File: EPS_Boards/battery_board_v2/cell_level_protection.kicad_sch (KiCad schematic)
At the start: 32 parts, among them J8 Shunt Resistor, Q10 CSD16401Q5, Q3 CSD16401Q5, Q4 CSD16401Q5, Q5 CSD16401Q5, Q6 CSD16401Q5, Q7 CSD16401Q5, Q8 CSD16401Q5, Q9 CSD16401Q5, U10 BQ297xx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

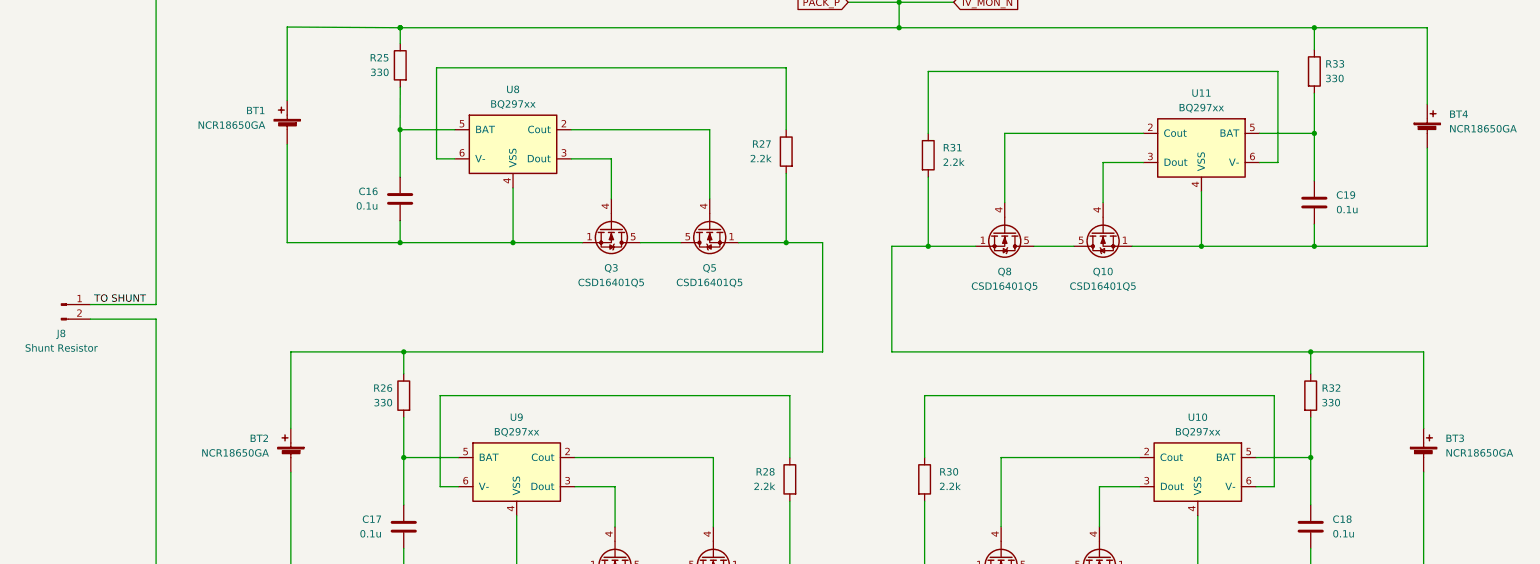
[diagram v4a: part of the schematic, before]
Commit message: eps: battery board: updated board layout
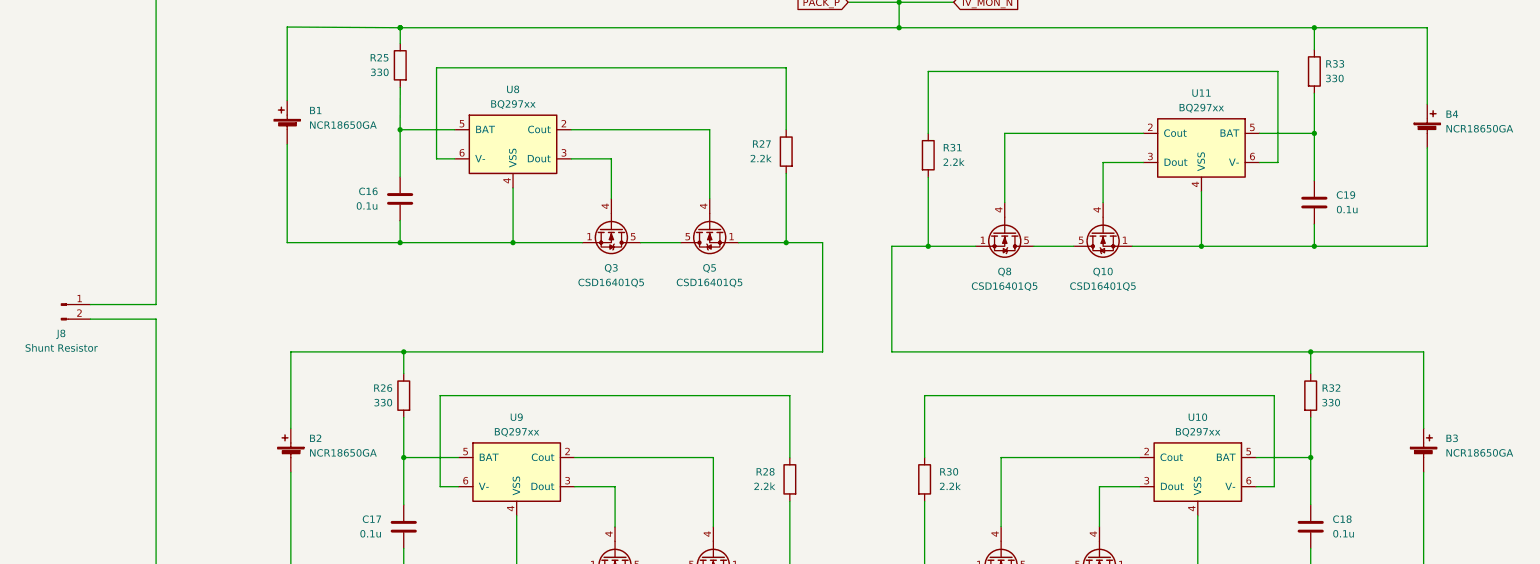
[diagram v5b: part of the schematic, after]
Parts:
- C16, C17, C18, C19: footprint (none) -> Capacitor_SMD:C_0402_1005Metric
- F1, F2: footprint (none) -> Capacitor_Tantalum_SMD:CP_EIA-7132-20_AVX-U_Pad2.72x3.50mm_HandSolder
- R25, R26, R27, R28, R29, R30, R31, R32, R33: footprint (none) -> Resistor_SMD:R_0402_1005Metric
- renumbered BT1 to B1, BT2 to B2, BT3 to B3, BT4 to B4
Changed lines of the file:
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@@
-    (effects (font (size 1.27 1.27)) (justify left bottom))
-  )
-  (label "TO SHUNT" (at 86.995 154.94 0)
     (effects (font (size 1.27 1.27)) (justify left bottom))
   )
@@
       (effects (font (size 1.27 1.27)) (justify left))
     )
-    (property "Footprint" "" (id 2) (at 210.058 185.42 90)
+    (property "Footprint" "Resistor_SMD:R_0402_1005Metric" (id 2) (at 210.058 185.42 90)
       (effects (font (size 1.27 1.27)) hide)
     )
@@
       (effects (font (size 1.27 1.27)) (justify right))
     )
-    (property "Footprint" "" (id 2) (at 298.7548 133.35 0)
+    (property "Footprint" "Capacitor_SMD:C_0402_1005Metric" (id 2) (at 298.7548 133.35 0)
       (effects (font (size 1.27 1.27)) hide)
     )
@@
       (effects (font (size 1.27 1.27)) (justify right))
     )
-    (property "Footprint" "" (id 2) (at 141.3002 132.715 0)
+    (property "Footprint" "Capacitor_SMD:C_0402_1005Metric" (id 2) (at 141.3002 132.715 0)
       (effects (font (size 1.27 1.27)) hide)
     )
@@
       (effects (font (size 1.27 1.27)) (justify left))
     )
-    (property "Footprint" "" (id 2) (at 297.307 170.815 90)
+    (property "Footprint" "Resistor_SMD:R_0402_1005Metric" (id 2) (at 297.307 170.815 90)
       (effects (font (size 1.27 1.27)) hide)
     )
@@
   (symbol (lib_id "Device:Battery_Cell") (at 121.285 181.61 0) (mirror y) (unit 1)
     (in_bom yes) (on_board yes) (fields_autoplaced)
-    (property "Reference" "BT2" (id 0) (at 117.475 178.3079 0)
-      (effects (font (size 1.27 1.27)) (justify left))
-    )
-    (property "Value" "NCR18650GA" (id 1) (at 117.475 180.8479 0)
-      (effects (font (size 1.27 1.27)) (justify left))
+    (property "Reference" "B2" (id 0) (at 124.46 178.3079 0)
+      (effects (font (size 1.27 1.27)) (justify right))
+    )
+    (property "Value" "NCR18650GA" (id 1) (at 124.46 180.8479 0)
+      (effects (font (size 1.27 1.27)) (justify right))
     )
     (property "Footprint" "qset-footprints:Keystone_54_18650" (id 2) (at 121.285 180.086 90)
@@
       (effects (font (size 1.27 1.27)) (justify left))
     )
-    (property "Footprint" "" (id 2) (at 297.942 114.3 90)
+    (property "Footprint" "Resistor_SMD:R_0402_1005Metric" (id 2) (at 297.942 114.3 90)
       (effects (font (size 1.27 1.27)) hide)
     )
@@
   (symbol (lib_id "Device:Battery_Cell") (at 318.77 181.61 0) (unit 1)
     (in_bom yes) (on_board yes) (fields_autoplaced)
-    (property "Reference" "BT3" (id 0) (at 322.58 178.3079 0)
+    (property "Reference" "B3" (id 0) (at 322.58 178.3079 0)
       (effects (font (size 1.27 1.27)) (justify left))
     )
@@
       (effects (font (size 1.27 1.27)) (justify left))
     )
-    (property "Footprint" "" (id 2) (at 229.997 185.42 90)
+    (property "Footprint" "Resistor_SMD:R_0402_1005Metric" (id 2) (at 229.997 185.42 90)
       (effects (font (size 1.27 1.27)) hide)
     )
@@
       (effects (font (size 1.27 1.27)) (justify left))
     )
-    (property "Footprint" "" (id 2) (at 230.632 128.905 90)
+    (property "Footprint" "Resistor_SMD:R_0402_1005Metric" (id 2) (at 230.632 128.905 90)
       (effects (font (size 1.27 1.27)) hide)
     )
@@
       (effects (font (size 1.27 1.27)) (justify right))
     )
-    (property "Footprint" "" (id 2) (at 141.9352 189.865 0)
+    (property "Footprint" "Capacitor_SMD:C_0402_1005Metric" (id 2) (at 141.9352 189.865 0)
       (effects (font (size 1.27 1.27)) hide)
     )
@@
       (effects (font (size 1.27 1.27)) (justify left))
     )
-    (property "Footprint" "" (id 2) (at 209.423 128.27 90)
+    (property "Footprint" "Resistor_SMD:R_0402_1005Metric" (id 2) (at 209.423 128.27 90)
       (effects (font (size 1.27 1.27)) hide)
     )
@@
       (effects (font (size 1.27 1.27)) (justify left))
     )
-    (property "Footprint" "" (id 2) (at 233.045 220.345 0)
-      (effects (font (size 1.27 1.27)) (justify left) hide)
-    )
-    (property "Datasheet" "~" (id 3) (at 231.775 215.265 0)
+    (property "Footprint" "Capacitor_Tantalum_SMD:CP_EIA-7132-20_AVX-U_Pad2.72x3.50mm_HandSolder" (id 2) (at 233.045 220.345 0)
+      (effects (font (size 1.27 1.27)) (justify left) hide)
+    )
+    (property "Datasheet" "" (id 3) (at 231.775 215.265 0)
       (effects (font (size 1.27 1.27)) hide)
     )
@@
       (effects (font (size 1.27 1.27)) (justify left))
     )
-    (property "Footprint" "" (id 2) (at 142.748 170.815 90)
+    (property "Footprint" "Resistor_SMD:R_0402_1005Metric" (id 2) (at 142.748 170.815 90)
       (effects (font (size 1.27 1.27)) hide)
     )
@@
       (effects (font (size 1.27 1.27)) (justify right))
     )
-    (property "Footprint" "" (id 2) (at 298.1198 189.865 0)
+    (property "Footprint" "Capacitor_SMD:C_0402_1005Metric" (id 2) (at 298.1198 189.865 0)
       (effects (font (size 1.27 1.27)) hide)
     )
@@
   (symbol (lib_id "Device:Battery_Cell") (at 319.405 125.095 0) (unit 1)
     (in_bom yes) (on_board yes) (fields_autoplaced)
-    (property "Reference" "BT4" (id 0) (at 323.215 121.7929 0)
-      (effects (font (size 1.27 1.27)) (justify left))
-    )
-    (property "Value" "NCR18650GA" (id 1) (at 323.215 124.3329 0)
+    (property "Reference" "B4" (id 0) (at 322.58 121.7929 0)
+      (effects (font (size 1.27 1.27)) (justify left))
+    )
+    (property "Value" "NCR18650GA" (id 1) (at 322.58 124.3329 0)
       (effects (font (size 1.27 1.27)) (justify left))
     )
@@
       (effects (font (size 1.27 1.27)) (justify left))
     )
-    (property "Footprint" "" (id 2) (at 225.552 94.615 90)
+    (property "Footprint" "Resistor_SMD:R_0402_1005Metric" (id 2) (at 225.552 94.615 90)
       (effects (font (size 1.27 1.27)) hide)
     )
@@
   (symbol (lib_id "Device:Battery_Cell") (at 120.65 124.46 0) (mirror y) (unit 1)
     (in_bom yes) (on_board yes) (fields_autoplaced)
-    (property "Reference" "BT1" (id 0) (at 116.84 121.1579 0)
-      (effects (font (size 1.27 1.27)) (justify left))
-    )
-    (property "Value" "NCR18650GA" (id 1) (at 116.84 123.6979 0)
-      (effects (font (size 1.27 1.27)) (justify left))
+    (property "Reference" "B1" (id 0) (at 124.46 121.1579 0)
+      (effects (font (size 1.27 1.27)) (justify right))
+    )
+    (property "Value" "NCR18650GA" (id 1) (at 124.46 123.6979 0)
+      (effects (font (size 1.27 1.27)) (justify right))
     )
     (property "Footprint" "qset-footprints:Keystone_54_18650" (id 2) (at 120.65 122.936 90)
@@
       (effects (font (size 1.27 1.27)) (justify left))
     )
-    (property "Footprint" "" (id 2) (at 209.55 220.345 0)
-      (effects (font (size 1.27 1.27)) (justify left) hide)
-    )
-    (property "Datasheet" "~" (id 3) (at 208.28 215.265 0)
+    (property "Footprint" "Capacitor_Tantalum_SMD:CP_EIA-7132-20_AVX-U_Pad2.72x3.50mm_HandSolder" (id 2) (at 209.55 220.345 0)
+      (effects (font (size 1.27 1.27)) (justify left) hide)
+    )
+    (property "Datasheet" "" (id 3) (at 208.28 215.265 0)
       (effects (font (size 1.27 1.27)) hide)
     )
@@
       (effects (font (size 1.27 1.27)) (justify left))
     )
-    (property "Footprint" "" (id 2) (at 142.1384 113.2332 90)
-      (effects (font (size 1.27 1.27)) hide)
-    )
+    (property "Footprint" "Resistor_SMD:R_0402_1005Metric" (id 2) (at 142.1384 113.2332 90)
+      (effects (font (size 1.27 1.27)) hide)
+    )

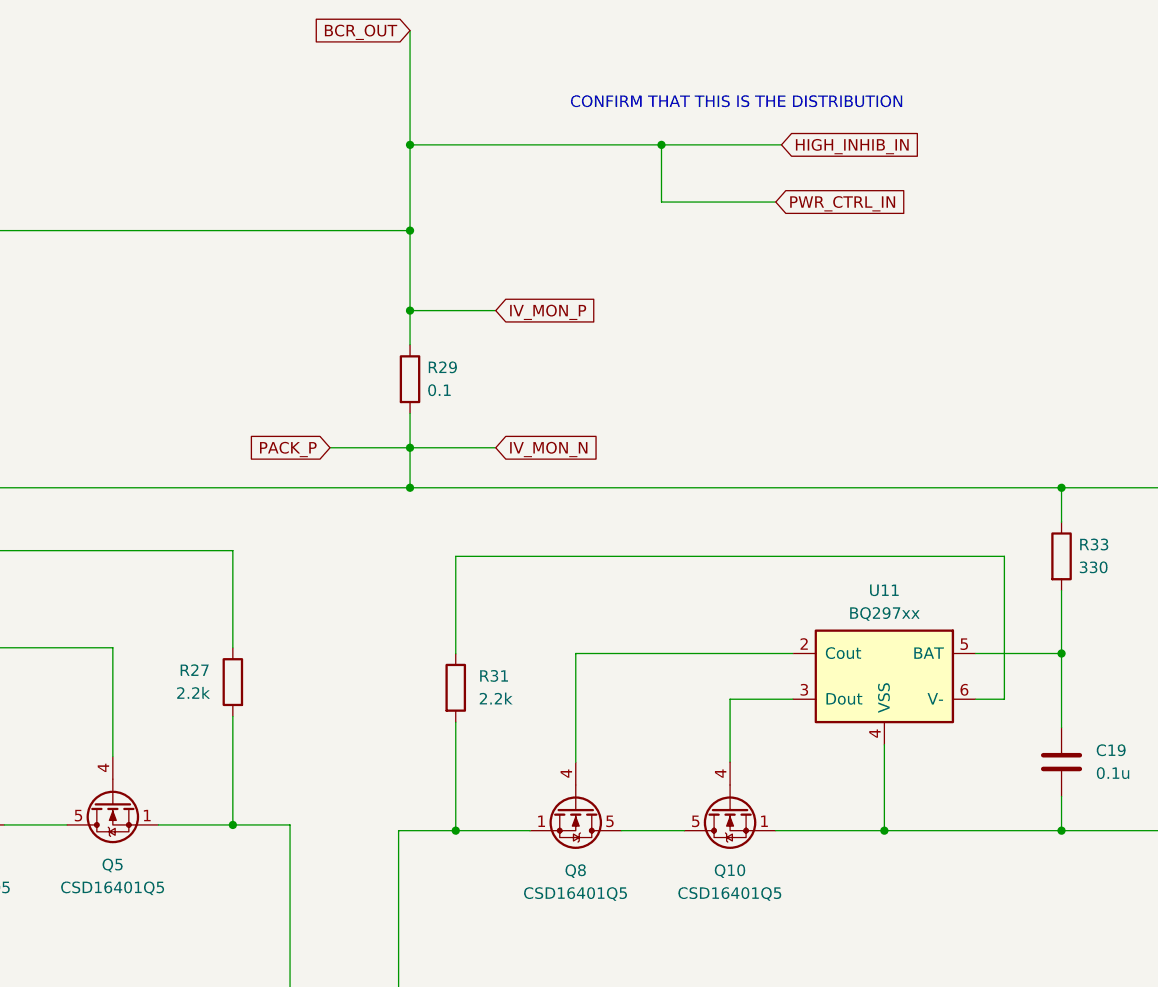
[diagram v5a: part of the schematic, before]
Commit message: eps: battery board: more updates to layout
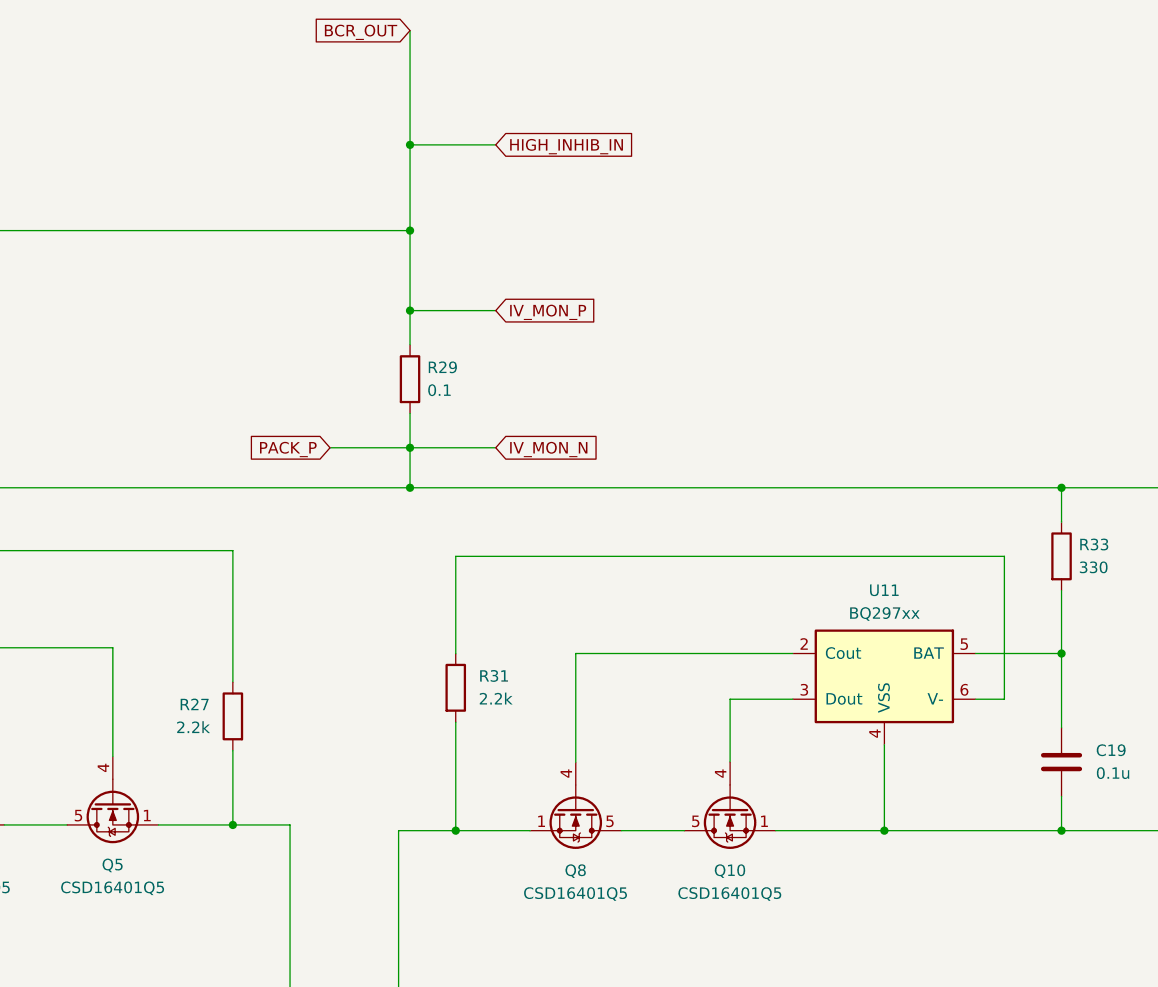
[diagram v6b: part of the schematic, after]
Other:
- note removed: "CONFIRM THAT THIS IS THE DISTRIBUTION"
- moved on the sheet: R27
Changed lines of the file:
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@@
   (junction (at 227.33 78.105) (diameter 0) (color 0 0 0 0)
   )
-  (junction (at 255.27 68.58) (diameter 0) (color 0 0 0 0)
-  )
   (junction (at 140.335 124.46) (diameter 0) (color 0 0 0 0)
   )
@@
     (stroke (width 0) (type default) (color 0 0 0 0))
   )
-  (wire (pts (xy 207.645 124.46) (xy 207.645 113.665))
+  (wire (pts (xy 207.645 128.27) (xy 207.645 113.665))
     (stroke (width 0) (type default) (color 0 0 0 0))
   )
@@
     (stroke (width 0) (type default) (color 0 0 0 0))
   )
-  (wire (pts (xy 255.27 74.93) (xy 267.97 74.93))
-    (stroke (width 0) (type default) (color 0 0 0 0))
-  )
   (wire (pts (xy 120.65 127) (xy 120.65 144.145))
     (stroke (width 0) (type default) (color 0 0 0 0))
@@
     (stroke (width 0) (type default) (color 0 0 0 0))
   )
-  (wire (pts (xy 227.33 68.58) (xy 255.27 68.58))
+  (wire (pts (xy 227.33 68.58) (xy 236.855 68.58))
     (stroke (width 0) (type default) (color 0 0 0 0))
   )
@@
     (stroke (width 0) (type default) (color 0 0 0 0))
   )
-  (wire (pts (xy 255.27 68.58) (xy 268.605 68.58))
-    (stroke (width 0) (type default) (color 0 0 0 0))
-  )
   (wire (pts (xy 189.865 201.295) (xy 182.88 201.295))
     (stroke (width 0) (type default) (color 0 0 0 0))
@@
     (stroke (width 0) (type default) (color 0 0 0 0))
   )
-  (wire (pts (xy 255.27 68.58) (xy 255.27 74.93))
-    (stroke (width 0) (type default) (color 0 0 0 0))
-  )
   (wire (pts (xy 299.085 174.625) (xy 299.085 181.61))
     (stroke (width 0) (type default) (color 0 0 0 0))
@@
     (stroke (width 0) (type default) (color 0 0 0 0))
   )
-  (wire (pts (xy 207.645 132.08) (xy 207.645 144.145))
+  (wire (pts (xy 207.645 135.89) (xy 207.645 144.145))
     (stroke (width 0) (type default) (color 0 0 0 0))
   )
@@
   (wire (pts (xy 120.65 106.553) (xy 120.65 119.38))
     (stroke (width 0) (type default) (color 0 0 0 0))
-  )
-  (text "CONFIRM THAT THIS IS THE DISTRIBUTION\n" (at 245.11 64.77 0)
-    (effects (font (size 1.27 1.27)) (justify left bottom))
   )
   (global_label "IV_MON_N" (shape input) (at 236.855 102.235 0) (fields_autoplaced)
@@
     )
   )
-  (global_label "PWR_CTRL_IN" (shape input) (at 267.97 74.93 0) (fields_autoplaced)
-    (effects (font (size 1.27 1.27)) (justify left))
-    (property "Intersheet References" "${INTERSHEET_REFS}" (id 0) (at 282.6918 74.8506 0)
-      (effects (font (size 1.27 1.27)) (justify left) hide)
-    )
-  )
   (global_label "PACK_P" (shape input) (at 218.44 102.235 180) (fields_autoplaced)
     (effects (font (size 1.27 1.27)) (justify right))
@@
     )
   )
-  (global_label "HIGH_INHIB_IN" (shape input) (at 268.605 68.58 0) (fields_autoplaced)
+  (global_label "HIGH_INHIB_IN" (shape input) (at 236.855 68.58 0) (fields_autoplaced)
     (effects (font (size 1.27 1.27)) (justify left))
-    (property "Intersheet References" "${INTERSHEET_REFS}" (id 0) (at 284.4759 68.5006 0)
+    (property "Intersheet References" "${INTERSHEET_REFS}" (id 0) (at 252.7259 68.5006 0)
       (effects (font (size 1.27 1.27)) (justify left) hide)
     )
@@
     (pin "2")
   )
-  (symbol (lib_id "Device:R") (at 207.645 128.27 0) (mirror y) (unit 1)
+  (symbol (lib_id "Device:R") (at 207.645 132.08 0) (mirror y) (unit 1)
     (in_bom yes) (on_board yes)
-    (property "Reference" "R27" (id 0) (at 205.105 126.9999 0)
-      (effects (font (size 1.27 1.27)) (justify left))
-    )
-    (property "Value" "2.2k" (id 1) (at 205.105 129.5399 0)
-      (effects (font (size 1.27 1.27)) (justify left))
-    )
-    (property "Footprint" "Resistor_SMD:R_0402_1005Metric" (id 2) (at 209.423 128.27 90)
-      (effects (font (size 1.27 1.27)) hide)
-    )
-    (property "Datasheet" "~" (id 3) (at 207.645 128.27 0)
-      (effects (font (size 1.27 1.27)) hide)
-    )
+    (property "Reference" "R27" (id 0) (at 205.105 130.8099 0)
+      (effects (font (size 1.27 1.27)) (justify left))
+    )
+    (property "Value" "2.2k" (id 1) (at 205.105 133.3499 0)
+      (effects (font (size 1.27 1.27)) (justify left))
+    )
+    (property "Footprint" "Resistor_SMD:R_0402_1005Metric" (id 2) (at 209.423 132.08 90)
+      (effects (font (size 1.27 1.27)) hide)
+    )
+    (property "Datasheet" "~" (id 3) (at 207.645 132.08 0)
+      (effects (font (size 1.27 1.27)) hide)
+    )
